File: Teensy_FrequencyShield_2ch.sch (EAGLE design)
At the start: 17 parts, among them IC9 78L05F

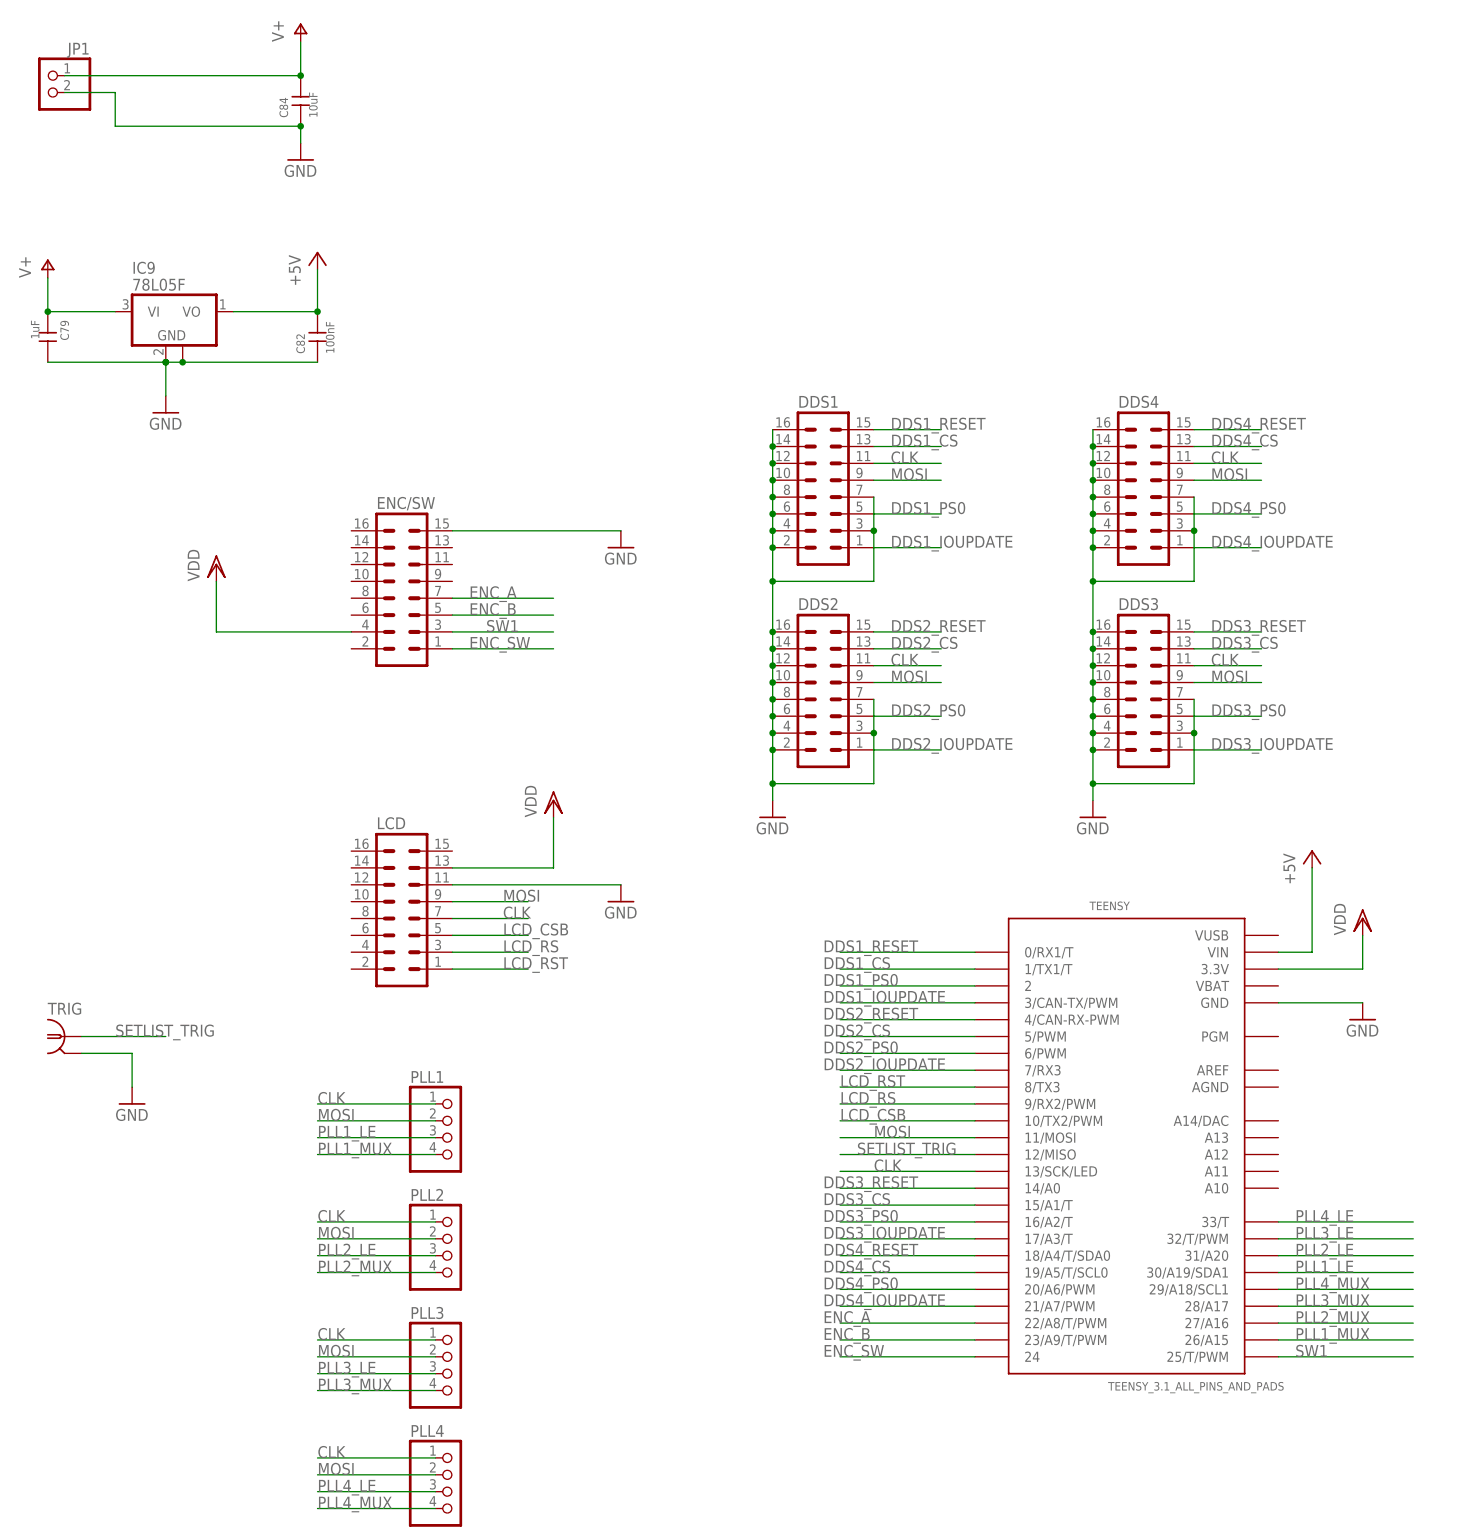
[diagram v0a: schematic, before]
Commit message: teensy board with two dds channels and 2 plls
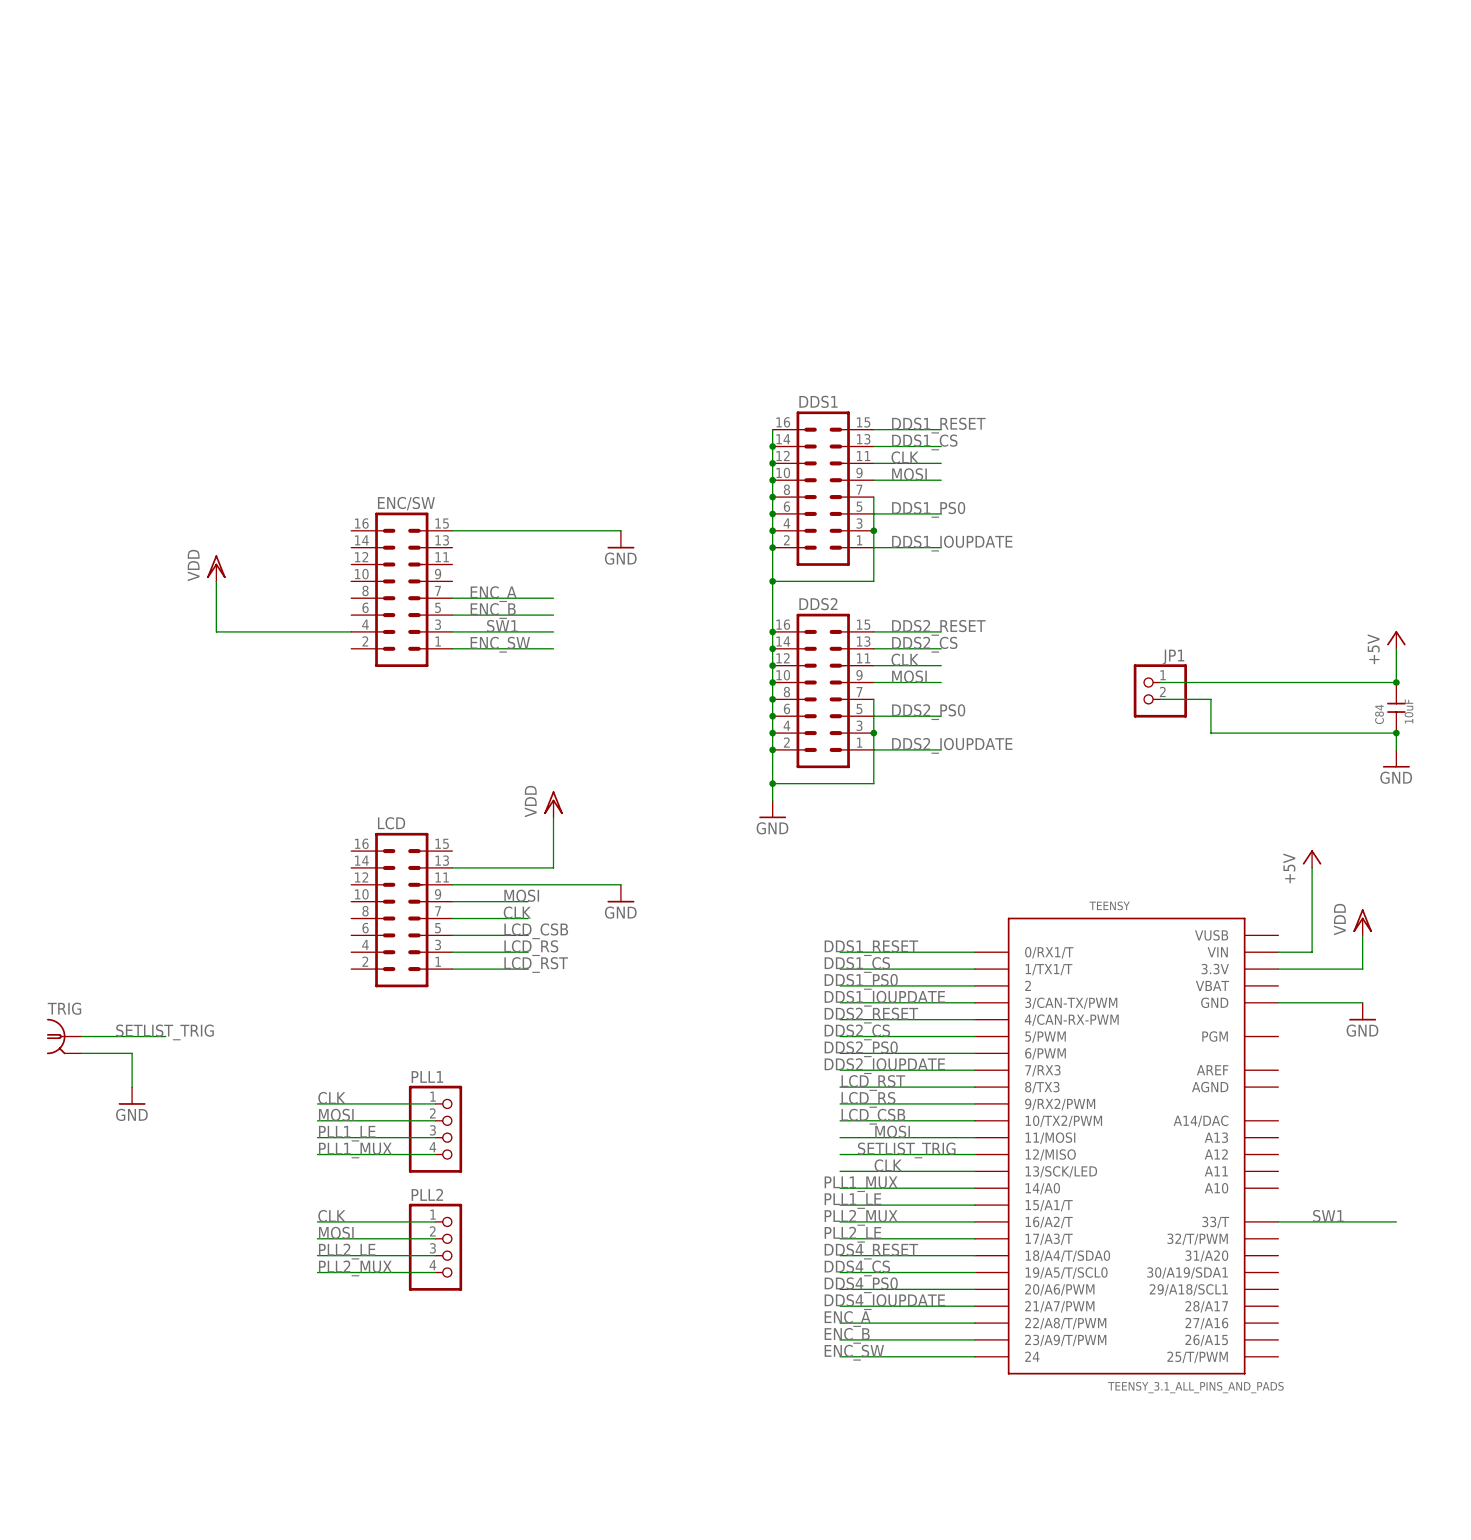
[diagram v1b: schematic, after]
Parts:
- removed C79: 1uF, rlc-jqi:CAP0805
- removed C82: 100nF, rlc-jqi:CAP0603
- removed DDS3, DDS4: (no value), mcu-accessories:ML16
- removed IC9: 78L05F, aom_driver:78L05F
- removed PLL3, PLL4: (no value), pinhead:PINHD-1X4
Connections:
- removed net DDS3_CS: DDS3.13, TEENSY.15/A1/T
- removed net DDS3_IOUPDATE: DDS3.1, TEENSY.17/A3/T
- removed net DDS3_PS0: DDS3.5, TEENSY.16/A2/T
- removed net DDS3_RESET: DDS3.15, TEENSY.14/A0
- removed net PLL3_LE: PLL3.3, TEENSY.32/T/PWM
- removed net PLL3_MUX: PLL3.4, TEENSY.28/A17
- removed net PLL4_LE: PLL4.3, TEENSY.33/T
- removed net PLL4_MUX: PLL4.4, TEENSY.29/A18/SCL1
- removed net V+: C79.P$1, C84.P$2, IC9.VI, JP1.1
- net +5V: now also C84.P$2, JP1.1; no longer C82.P$2, IC9.VO
- net CLK: no longer DDS3.11, DDS4.11, PLL3.1, PLL4.1
- net DDS4_CS: no longer DDS4.13
- net DDS4_IOUPDATE: no longer DDS4.1
- net DDS4_PS0: no longer DDS4.5
- net DDS4_RESET: no longer DDS4.15
- net GND: no longer C79.P$2, C82.P$1, DDS3.10, DDS3.12, DDS3.14, DDS3.16, DDS3.2, DDS3.3, DDS3.4, DDS3.6, DDS3.7, DDS3.8, DDS4.10, DDS4.12, DDS4.14, DDS4.16, DDS4.2, DDS4.3, DDS4.4, DDS4.6, DDS4.7, DDS4.8, IC9.GND, IC9.GND@1
- net MOSI: no longer DDS3.9, DDS4.9, PLL3.2, PLL4.2
- net PLL1_LE: now also TEENSY.15/A1/T; no longer TEENSY.30/A19/SDA1
- net PLL1_MUX: now also TEENSY.14/A0; no longer TEENSY.26/A15
- net PLL2_LE: now also TEENSY.17/A3/T; no longer TEENSY.31/A20
- net PLL2_MUX: now also TEENSY.16/A2/T; no longer TEENSY.27/A16
- net SW1: now also TEENSY.33/T; no longer TEENSY.25/T/PWM
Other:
- moved on the sheet: C84, JP1

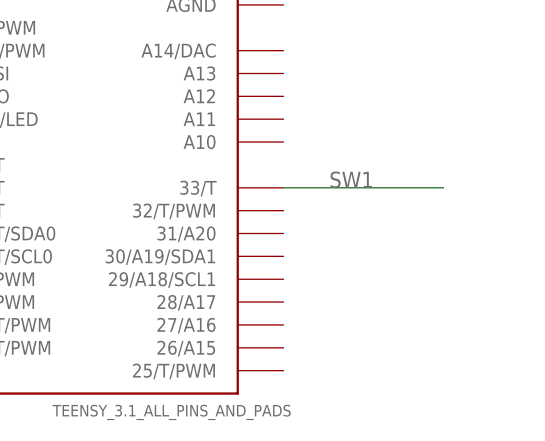
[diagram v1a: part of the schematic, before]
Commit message: Tweaked pin layout; added back in extra DDS & PLL channel names to Teensy pinout
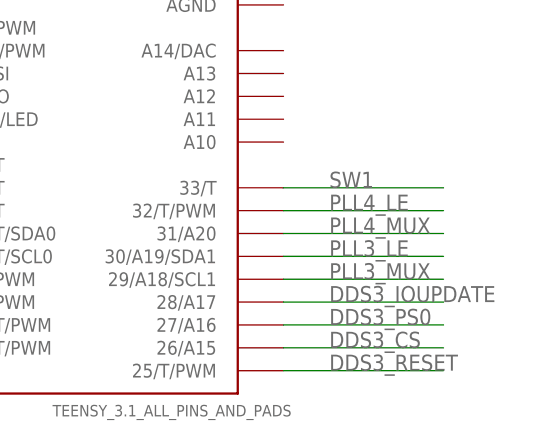
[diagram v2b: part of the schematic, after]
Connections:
- new net DDS3_CS: TEENSY.26/A15
- new net DDS3_IOUPDATE: TEENSY.28/A17
- new net DDS3_PS0: TEENSY.27/A16
- new net DDS3_RESET: TEENSY.25/T/PWM
- new net PLL3_LE: TEENSY.30/A19/SDA1
- new net PLL3_MUX: TEENSY.29/A18/SCL1
- new net PLL4_LE: TEENSY.32/T/PWM
- new net PLL4_MUX: TEENSY.31/A20
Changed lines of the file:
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@@
 <?xml version="1.0" encoding="utf-8"?>
 <!DOCTYPE eagle SYSTEM "eagle.dtd">
-<eagle version="6.2">
+<eagle version="6.5.0">
 <drawing>
 <settings>
@@
 <setting verticaltext="up"/>
 </settings>
-<grid distance="0.1" unitdist="inch" unit="inch" style="lines" multiple="1" display="no" altdistance="0.01" altunitdist="inch" altunit="inch"/>
+<grid distance="0.05" unitdist="inch" unit="inch" style="lines" multiple="1" display="no" altdistance="0.01" altunitdist="inch" altunit="inch"/>
 <layers>
 <layer number="1" name="Top" color="4" fill="1" visible="no" active="no"/>
@@
 </segment>
 </net>
+<net name="DDS3_RESET" class="0">
+<segment>
+<pinref part="TEENSY" gate="G$1" pin="25/T/PWM"/>
+<wire x1="93.98" y1="22.86" x2="111.76" y2="22.86" width="0.1524" layer="91"/>
+<label x="99.06" y="22.86" size="1.778" layer="95"/>
+</segment>
+</net>
+<net name="DDS3_CS" class="0">
+<segment>
+<pinref part="TEENSY" gate="G$1" pin="26/A15"/>
+<wire x1="93.98" y1="25.4" x2="111.76" y2="25.4" width="0.1524" layer="91"/>
+<label x="99.06" y="25.4" size="1.778" layer="95"/>
+</segment>
+</net>
+<net name="DDS3_PS0" class="0">
+<segment>
+<pinref part="TEENSY" gate="G$1" pin="27/A16"/>
+<wire x1="93.98" y1="27.94" x2="111.76" y2="27.94" width="0.1524" layer="91"/>
+<label x="99.06" y="27.94" size="1.778" layer="95"/>
+</segment>
+</net>
+<net name="DDS3_IOUPDATE" class="0">
+<segment>
+<pinref part="TEENSY" gate="G$1" pin="28/A17"/>
+<wire x1="93.98" y1="30.48" x2="111.76" y2="30.48" width="0.1524" layer="91"/>
+<label x="99.06" y="30.48" size="1.778" layer="95"/>
+</segment>
+</net>
+<net name="PLL3_LE" class="0">
+<segment>
+<pinref part="TEENSY" gate="G$1" pin="30/A19/SDA1"/>
+<wire x1="93.98" y1="35.56" x2="111.76" y2="35.56" width="0.1524" layer="91"/>
+<label x="99.06" y="35.56" size="1.778" layer="95"/>
+</segment>
+</net>
+<net name="PLL4_MUX" class="0">
+<segment>
+<pinref part="TEENSY" gate="G$1" pin="31/A20"/>
+<wire x1="93.98" y1="38.1" x2="111.76" y2="38.1" width="0.1524" layer="91"/>
+<label x="99.06" y="38.1" size="1.778" layer="95"/>
+</segment>
+</net>
+<net name="PLL4_LE" class="0">
+<segment>
+<pinref part="TEENSY" gate="G$1" pin="32/T/PWM"/>
+<wire x1="93.98" y1="40.64" x2="111.76" y2="40.64" width="0.1524" layer="91"/>
+<label x="99.06" y="40.64" size="1.778" layer="95"/>
+</segment>
+</net>
+<net name="PLL3_MUX" class="0">
+<segment>
+<pinref part="TEENSY" gate="G$1" pin="29/A18/SCL1"/>
+<wire x1="93.98" y1="33.02" x2="111.76" y2="33.02" width="0.1524" layer="91"/>
+<label x="99.06" y="33.02" size="1.778" layer="95"/>
+</segment>
+</net>

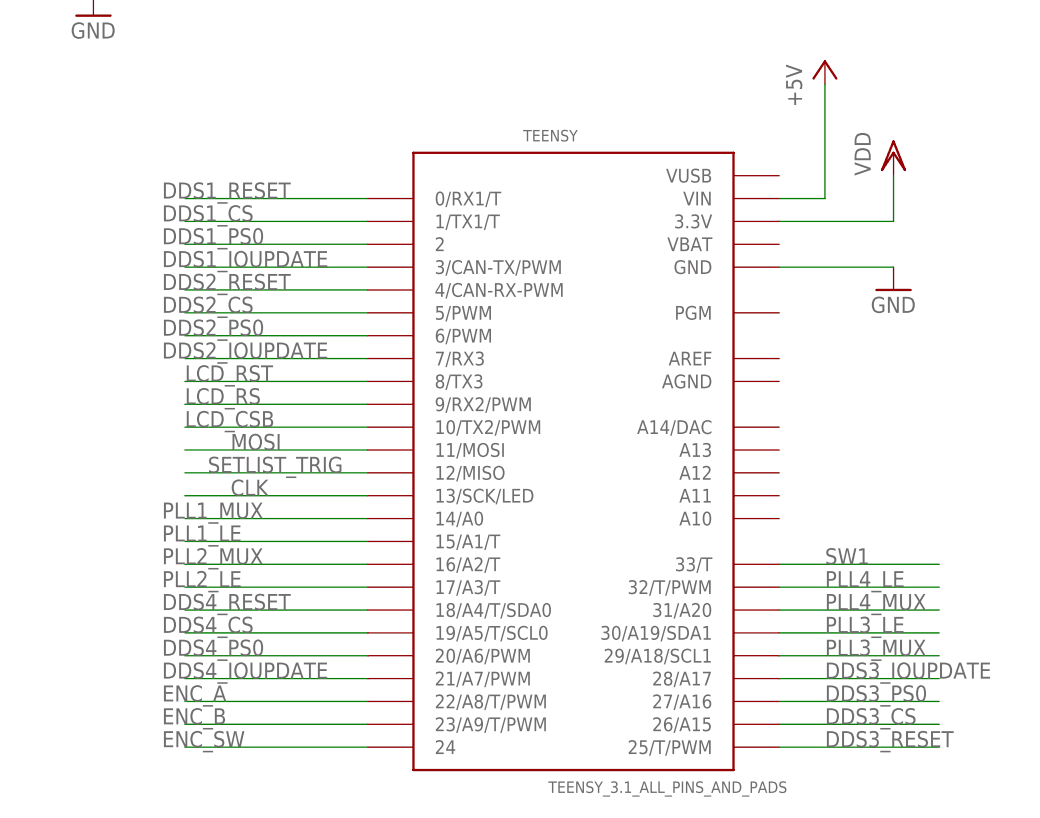
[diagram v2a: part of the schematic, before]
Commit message: Re-routed Teensy_FreqShield to be a (mostly) 1-layer board
* Easier printing on LKPF machine
* GND connected through a few rivets to the top layer
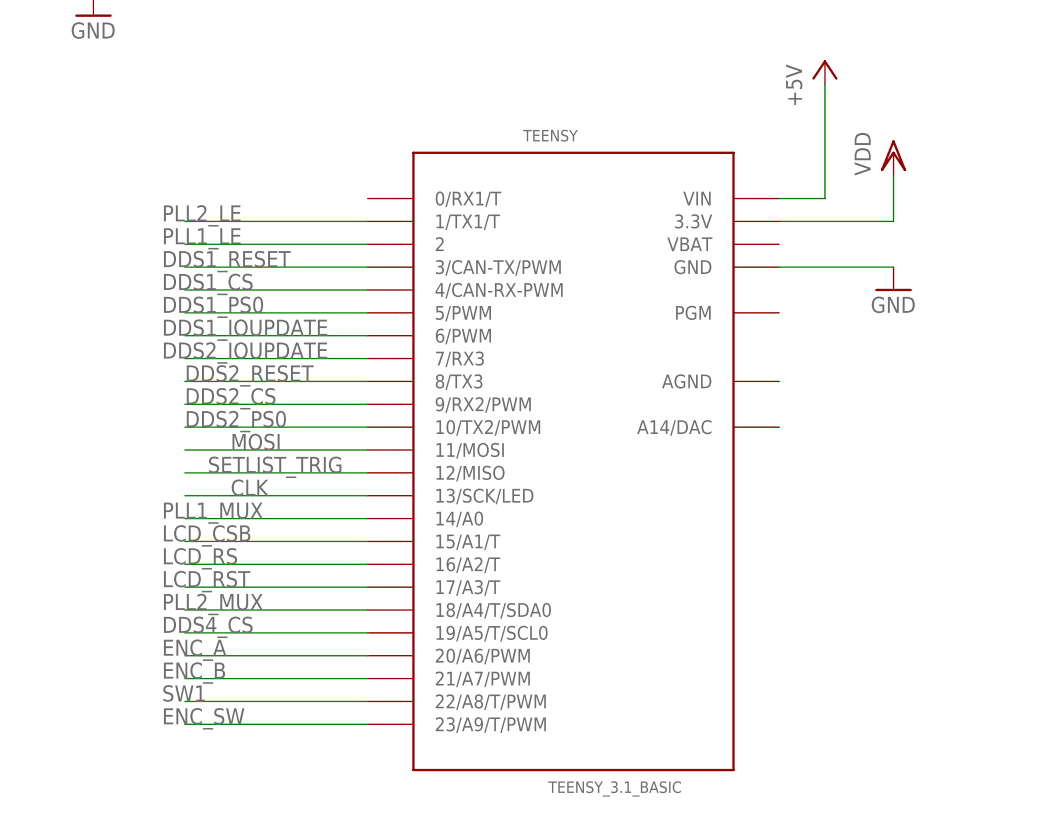
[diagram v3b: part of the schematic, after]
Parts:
- TEENSY: value TEENSY_3.1_ALL_PINS_AND_PADS -> TEENSY_3.1_BASIC; device mcu-accessories:TEENSY_3.1_ALL_PINS_AND_PADS -> mcu-accessories:TEENSY_3.1_BASIC
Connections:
- removed net DDS3_CS: TEENSY.26/A15
- removed net DDS3_IOUPDATE: TEENSY.28/A17
- removed net DDS3_PS0: TEENSY.27/A16
- removed net DDS3_RESET: TEENSY.25/T/PWM
- removed net DDS4_IOUPDATE: TEENSY.21/A7/PWM
- removed net DDS4_PS0: TEENSY.20/A6/PWM
- removed net DDS4_RESET: TEENSY.18/A4/T/SDA0
- removed net PLL3_LE: TEENSY.30/A19/SDA1
- removed net PLL3_MUX: TEENSY.29/A18/SCL1
- removed net PLL4_LE: TEENSY.32/T/PWM
- removed net PLL4_MUX: TEENSY.31/A20
- net DDS1_CS: now also TEENSY.4/CAN-RX-PWM; no longer TEENSY.1/TX1/T
- net DDS1_IOUPDATE: now also TEENSY.6/PWM; no longer TEENSY.3/CAN-TX/PWM
- net DDS1_PS0: now also TEENSY.5/PWM; no longer TEENSY.2
- net DDS1_RESET: now also TEENSY.3/CAN-TX/PWM; no longer TEENSY.0/RX1/T
- net DDS2_CS: now also TEENSY.9/RX2/PWM; no longer TEENSY.5/PWM
- net DDS2_PS0: now also TEENSY.10/TX2/PWM; no longer TEENSY.6/PWM
- net DDS2_RESET: now also TEENSY.8/TX3; no longer TEENSY.4/CAN-RX-PWM
- net ENC_A: now also TEENSY.20/A6/PWM; no longer TEENSY.22/A8/T/PWM
- net ENC_B: now also TEENSY.21/A7/PWM; no longer TEENSY.23/A9/T/PWM
- net ENC_SW: now also TEENSY.23/A9/T/PWM; no longer TEENSY.24
- net LCD_CSB: now also TEENSY.15/A1/T; no longer TEENSY.10/TX2/PWM
- net LCD_RS: now also TEENSY.16/A2/T; no longer TEENSY.9/RX2/PWM
- net LCD_RST: now also TEENSY.17/A3/T; no longer TEENSY.8/TX3
- net PLL1_LE: now also TEENSY.2; no longer TEENSY.15/A1/T
- net PLL2_LE: now also TEENSY.1/TX1/T; no longer TEENSY.17/A3/T
- net PLL2_MUX: now also TEENSY.18/A4/T/SDA0; no longer TEENSY.16/A2/T
- net SW1: now also TEENSY.22/A8/T/PWM; no longer TEENSY.33/T
